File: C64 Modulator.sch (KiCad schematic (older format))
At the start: 29 parts, among them J1 Power, J2 8765, J3 4321, J4 AUD_STEREO, J5 TRS_3.5mm, J6 RCA_PLUG, Q1 BC549, Q2 BC549

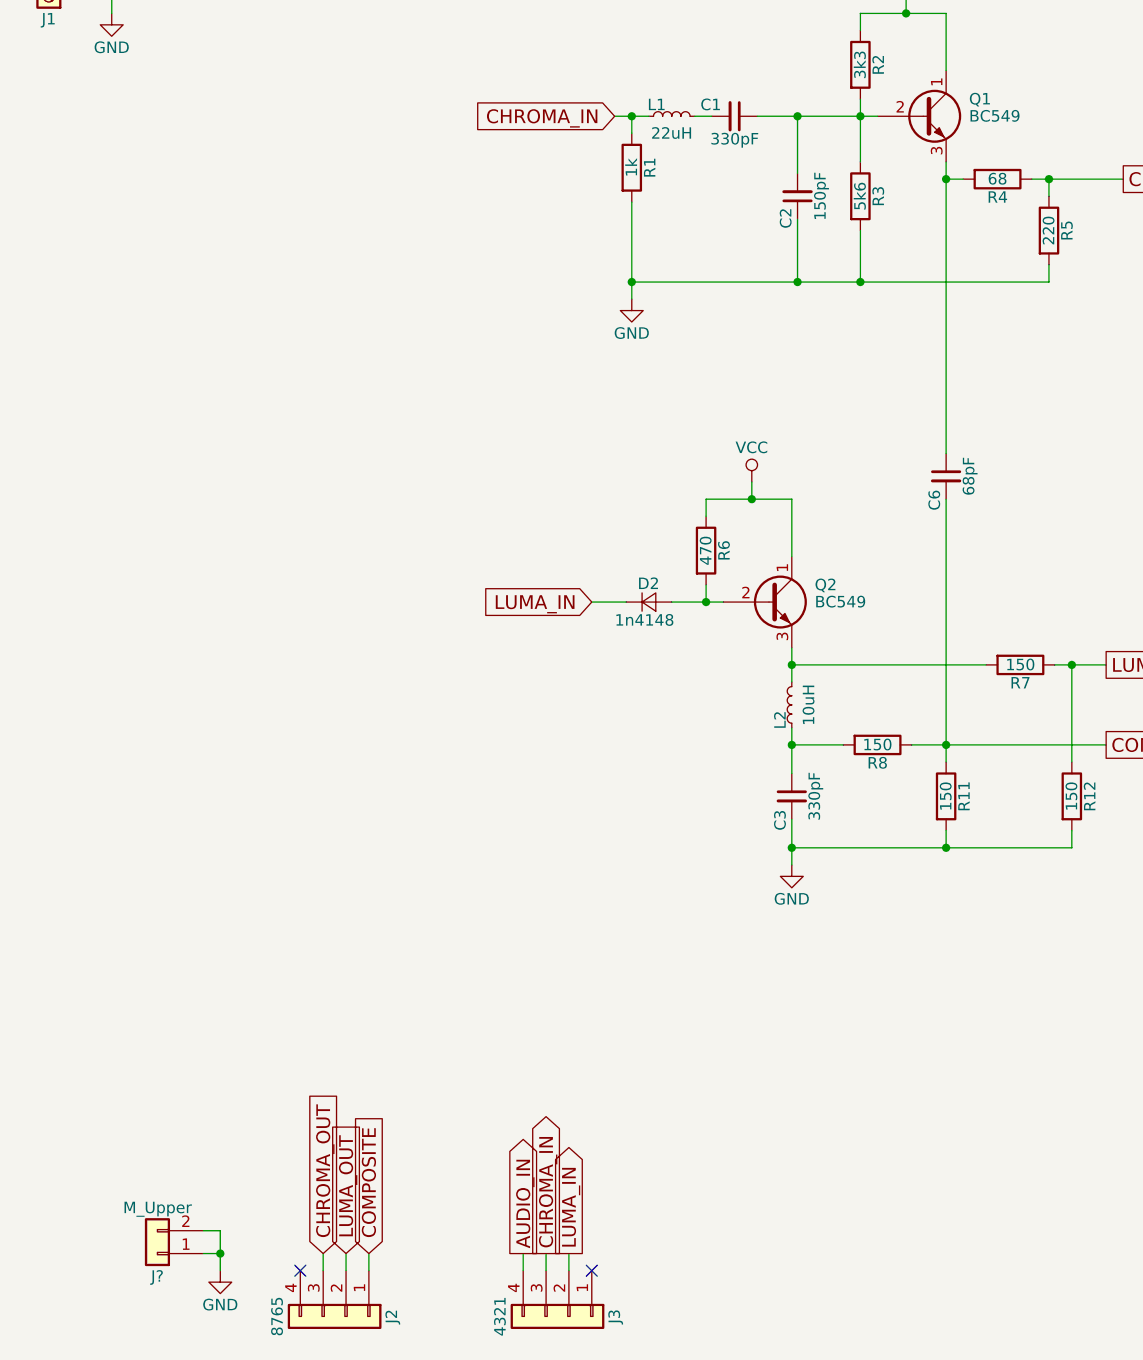
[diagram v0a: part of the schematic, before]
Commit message: Assigned footprints
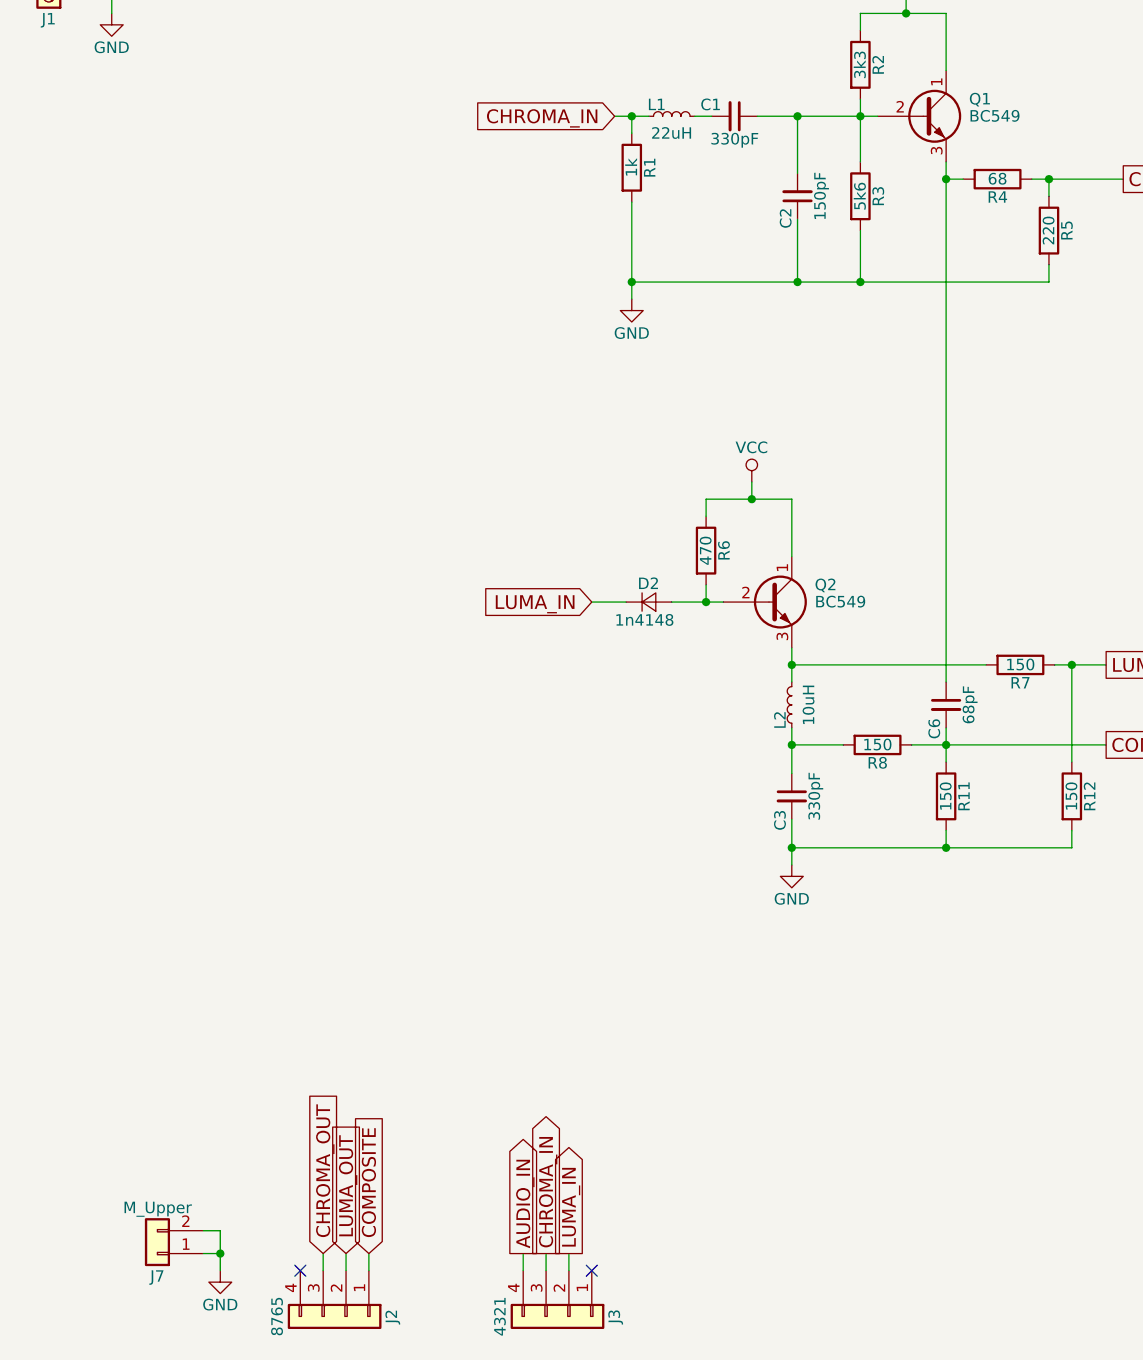
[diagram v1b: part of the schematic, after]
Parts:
- C1, C2, C3, C6: footprint (none) -> Capacitors_THT:C_Disc_D4.7mm_W2.5mm_P5.00mm
- D1, D2: footprint (none) -> Diodes_THT:D_DO-35_SOD27_P7.62mm_Horizontal
- J1, JP1: footprint (none) -> Pin_Headers:Pin_Header_Straight_1x02_Pitch2.54mm
- J2, J3: footprint (none) -> Pin_Headers:Pin_Header_Straight_1x04_Pitch2.54mm
- J4: footprint (none) -> Pin_Headers:Pin_Header_Straight_1x01_Pitch2.54mm
- J5: footprint (none) -> trs:Tayda_3.5mm_stereo_TRS_jack_A-853
- J6: footprint (none) -> rca:rca_yellow
- J7: renamed from J?; footprint (none) -> Pin_Headers:Pin_Header_Straight_1x02_Pitch2.54mm
- JP2: footprint (none) -> Pin_Headers:Pin_Header_Straight_1x03_Pitch2.54mm
- L1, L2: footprint (none) -> Inductors_THT:L_Axial_L6.6mm_D2.7mm_P10.16mm_Horizontal_Vishay_IM-2
- R1, R11, R12, R2, R3, R4, R5, R6, R7, R8: footprint (none) -> Resistors_THT:R_Axial_DIN0207_L6.3mm_D2.5mm_P10.16mm_Horizontal
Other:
- moved on the sheet: C6
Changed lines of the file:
@@
 F 0 "R2" V 5655 1350 50  0000 C CNN
 F 1 "3k3" V 5575 1350 50  0000 C CNN
-F 2 "" V 5505 1350 50  0001 C CNN
+F 2 "Resistors_THT:R_Axial_DIN0207_L6.3mm_D2.5mm_P10.16mm_Horizontal" V 5505 1350 50  0001 C CNN
 F 3 "" H 5575 1350 50  0001 C CNN
 	1    5575 1350
@@
 F 0 "R3" V 5655 1925 50  0000 C CNN
 F 1 "5k6" V 5575 1925 50  0000 C CNN
-F 2 "" V 5505 1925 50  0001 C CNN
+F 2 "Resistors_THT:R_Axial_DIN0207_L6.3mm_D2.5mm_P10.16mm_Horizontal" V 5505 1925 50  0001 C CNN
 F 3 "" H 5575 1925 50  0001 C CNN
 	1    5575 1925
@@
 F 0 "C1" V 4975 1425 50  0000 L CNN
 F 1 "330pF" V 5125 1575 50  0000 C CNN
-F 2 "" H 5025 1575 50  0001 C CNN
+F 2 "Capacitors_THT:C_Disc_D4.7mm_W2.5mm_P5.00mm" H 5025 1575 50  0001 C CNN
 F 3 "" H 5025 1575 50  0001 C CNN
 	1    5025 1575
@@
 F 0 "L1" V 4800 1600 50  0000 L CNN
 F 1 "22uH" V 4675 1575 50  0000 C CNN
-F 2 "" H 4750 1575 50  0001 C CNN
+F 2 "Inductors_THT:L_Axial_L6.6mm_D2.7mm_P10.16mm_Horizontal_Vishay_IM-2" H 4750 1575 50  0001 C CNN
 F 3 "" H 4750 1575 50  0001 C CNN
 	1    4750 1575
@@
 F 0 "R1" V 4655 1800 50  0000 C CNN
 F 1 "1k" V 4575 1800 50  0000 C CNN
-F 2 "" V 4505 1800 50  0001 C CNN
+F 2 "Resistors_THT:R_Axial_DIN0207_L6.3mm_D2.5mm_P10.16mm_Horizontal" V 4505 1800 50  0001 C CNN
 F 3 "" H 4575 1800 50  0001 C CNN
 	1    4575 1800
@@
 F 0 "C2" V 5350 1975 50  0000 L CNN
 F 1 "150pF" V 5200 1925 50  0000 C CNN
-F 2 "" H 5300 1925 50  0001 C CNN
+F 2 "Capacitors_THT:C_Disc_D4.7mm_W2.5mm_P5.00mm" H 5300 1925 50  0001 C CNN
 F 3 "" H 5300 1925 50  0001 C CNN
 	1    5300 1925
@@
 F 0 "R4" V 6255 1850 50  0000 C CNN
 F 1 "68" V 6175 1850 50  0000 C CNN
-F 2 "" V 6105 1850 50  0001 C CNN
+F 2 "Resistors_THT:R_Axial_DIN0207_L6.3mm_D2.5mm_P10.16mm_Horizontal" V 6105 1850 50  0001 C CNN
 F 3 "" H 6175 1850 50  0001 C CNN
 	1    6175 1850
@@
 $EndComp
 Wire Wire Line
-	5950 1775 5950 3050
+	5950 1775 5950 4050
 Wire Wire Line
 	5950 1850 6025 1850
@@
 F 0 "R5" V 6480 2075 50  0000 C CNN
 F 1 "220" V 6400 2075 50  0000 C CNN
-F 2 "" V 6330 2075 50  0001 C CNN
+F 2 "Resistors_THT:R_Axial_DIN0207_L6.3mm_D2.5mm_P10.16mm_Horizontal" V 6330 2075 50  0001 C CNN
 F 3 "" H 6400 2075 50  0001 C CNN
 	1    6400 2075
@@
 F 0 "R6" V 4980 3475 50  0000 C CNN
 F 1 "470" V 4900 3475 50  0000 C CNN
-F 2 "" V 4830 3475 50  0001 C CNN
+F 2 "Resistors_THT:R_Axial_DIN0207_L6.3mm_D2.5mm_P10.16mm_Horizontal" V 4830 3475 50  0001 C CNN
 F 3 "" H 4900 3475 50  0001 C CNN
 	1    4900 3475
@@
 F 0 "D2" H 4600 3780 50  0000 L CNN
 F 1 "1n4148" H 4500 3620 50  0000 L CNN
-F 2 "" V 4650 3700 50  0001 C CNN
+F 2 "Diodes_THT:D_DO-35_SOD27_P7.62mm_Horizontal" V 4650 3700 50  0001 C CNN
 F 3 "" V 4650 3700 50  0001 C CNN
 	1    4650 3700
@@
 F 0 "L2" V 5325 4175 50  0000 L CNN
 F 1 "10uH" V 5200 4150 50  0000 C CNN
-F 2 "" H 5275 4150 50  0001 C CNN
+F 2 "Inductors_THT:L_Axial_L6.6mm_D2.7mm_P10.16mm_Horizontal_Vishay_IM-2" H 5275 4150 50  0001 C CNN
 F 3 "" H 5275 4150 50  0001 C CNN
 	1    5275 4150
@@
 F 0 "D1" H 2350 1030 50  0000 L CNN
 F 1 "1n4148" H 2250 870 50  0000 L CNN
-F 2 "" V 2400 950 50  0001 C CNN
+F 2 "Diodes_THT:D_DO-35_SOD27_P7.62mm_Horizontal" V 2400 950 50  0001 C CNN
 F 3 "" V 2400 950 50  0001 C CNN
 	1    2400 950
@@
 F 0 "C3" V 5225 4400 50  0000 L CNN
 F 1 "330pF" V 5375 4550 50  0000 C CNN
-F 2 "" H 5275 4550 50  0001 C CNN
+F 2 "Capacitors_THT:C_Disc_D4.7mm_W2.5mm_P5.00mm" H 5275 4550 50  0001 C CNN
 F 3 "" H 5275 4550 50  0001 C CNN
 	1    5275 4550
@@
 F 0 "J1" H 2025 1150 50  0000 C CNN
 F 1 "Power" H 2025 850 50  0000 C CNN
-F 2 "" H 2025 1050 50  0001 C CNN
+F 2 "Pin_Headers:Pin_Header_Straight_1x02_Pitch2.54mm" H 2025 1050 50  0001 C CNN
 F 3 "" H 2025 1050 50  0001 C CNN
 	1    2025 1050
@@
 L C_Small C6
 U 1 1 5D0D1EC2
-P 5950 3150
-F 0 "C6" V 5900 3000 50  0000 L CNN
-F 1 "68pF" V 6050 3150 50  0000 C CNN
-F 2 "" H 5950 3150 50  0001 C CNN
-F 3 "" H 5950 3150 50  0001 C CNN
-	1    5950 3150
+P 5950 4150
+F 0 "C6" V 5900 4000 50  0000 L CNN
+F 1 "68pF" V 6050 4150 50  0000 C CNN
+F 2 "Capacitors_THT:C_Disc_D4.7mm_W2.5mm_P5.00mm" H 5950 4150 50  0001 C CNN
+F 3 "" H 5950 4150 50  0001 C CNN
+	1    5950 4150
 	1    0    0    -1
 $EndComp
@@
 F 0 "R11" V 6030 4550 50  0000 C CNN
 F 1 "150" V 5950 4550 50  0000 C CNN
-F 2 "" V 5880 4550 50  0001 C CNN
+F 2 "Resistors_THT:R_Axial_DIN0207_L6.3mm_D2.5mm_P10.16mm_Horizontal" V 5880 4550 50  0001 C CNN
 F 3 "" H 5950 4550 50  0001 C CNN
 	1    5950 4550
@@
 F 0 "R12" V 6580 4550 50  0000 C CNN
 F 1 "150" V 6500 4550 50  0000 C CNN
-F 2 "" V 6430 4550 50  0001 C CNN
+F 2 "Resistors_THT:R_Axial_DIN0207_L6.3mm_D2.5mm_P10.16mm_Horizontal" V 6430 4550 50  0001 C CNN
 F 3 "" H 6500 4550 50  0001 C CNN
 	1    6500 4550
@@
 F 0 "R8" V 5730 4325 50  0000 C CNN
 F 1 "150" V 5650 4325 50  0000 C CNN
-F 2 "" V 5580 4325 50  0001 C CNN
+F 2 "Resistors_THT:R_Axial_DIN0207_L6.3mm_D2.5mm_P10.16mm_Horizontal" V 5580 4325 50  0001 C CNN
 F 3 "" H 5650 4325 50  0001 C CNN
 	1    5650 4325
@@
 $EndComp
 Wire Wire Line
-	5950 3250 5950 4400
+	5950 4250 5950 4400
 Wire Wire Line
 	5800 4325 6650 4325
@@
 F 0 "R7" V 6355 3975 50  0000 C CNN
 F 1 "150" V 6275 3975 50  0000 C CNN
-F 2 "" V 6205 3975 50  0001 C CNN
+F 2 "Resistors_THT:R_Axial_DIN0207_L6.3mm_D2.5mm_P10.16mm_Horizontal" V 6205 3975 50  0001 C CNN
 F 3 "" H 6275 3975 50  0001 C CNN
 	1    6275 3975
@@
 F 0 "J3" H 4300 7025 50  0000 C CNN
 F 1 "4321" H 4300 6525 50  0000 C CNN
-F 2 "" H 4300 6825 50  0001 C CNN
+F 2 "Pin_Headers:Pin_Header_Straight_1x04_Pitch2.54mm" H 4300 6825 50  0001 C CNN
 F 3 "" H 4300 6825 50  0001 C CNN
 	1    4300 6825
@@
 F 0 "J2" H 3325 7025 50  0000 C CNN
 F 1 "8765" H 3325 6525 50  0000 C CNN
-F 2 "" H 3325 6825 50  0001 C CNN
+F 2 "Pin_Headers:Pin_Header_Straight_1x04_Pitch2.54mm" H 3325 6825 50  0001 C CNN
 F 3 "" H 3325 6825 50  0001 C CNN
 	1    3325 6825
@@
 F 0 "J6" H 10485 1420 50  0000 C CNN
 F 1 "RCA_PLUG" V 10590 1300 50  0000 C CNN
-F 2 "" H 10475 1300 50  0001 C CNN
+F 2 "rca:rca_yellow" H 10475 1300 50  0001 C CNN
 F 3 "" H 10475 1300 50  0001 C CNN
 	1    10475 1300
@@
 F 0 "J5" H 10275 2140 50  0000 C CNN
 F 1 "TRS_3.5mm" H 10125 1650 50  0000 L CNN
-F 2 "" H 10525 1950 50  0001 C CNN
+F 2 "trs:Tayda_3.5mm_stereo_TRS_jack_A-853" H 10525 1950 50  0001 C CNN
 F 3 "" H 10525 1950 50  0001 C CNN
 	1    10275 1850
@@
 F 0 "J4" H 9700 2675 50  0000 C CNN
 F 1 "AUD_STEREO" H 9700 2475 50  0000 C CNN
-F 2 "" H 9700 2575 50  0001 C CNN
+F 2 "Pin_Headers:Pin_Header_Straight_1x01_Pitch2.54mm" H 9700 2575 50  0001 C CNN
 F 3 "" H 9700 2575 50  0001 C CNN
 	1    9700 2575
@@
 F 0 "JP1" H 9200 1930 50  0000 C CNN
 F 1 "AUD_SEL" H 9210 1790 50  0000 C CNN
-F 2 "" H 9200 1850 50  0001 C CNN
+F 2 "Pin_Headers:Pin_Header_Straight_1x02_Pitch2.54mm" H 9200 1850 50  0001 C CNN
 F 3 "" H 9200 1850 50  0001 C CNN
 	1    9200 1850
@@
 F 0 "JP2" H 9750 2100 50  0000 L CNN
 F 1 "AUD_JOIN" H 9700 2300 50  0000 C BNN
-F 2 "" H 9700 2200 50  0001 C CNN
+F 2 "Pin_Headers:Pin_Header_Straight_1x03_Pitch2.54mm" H 9700 2200 50  0001 C CNN
 F 3 "" H 9700 2200 50  0001 C CNN
 	1    9700 2200
@@
 	10025 2575 9900 2575
 $Comp
-L Conn_01x02 J?
+L Conn_01x02 J7
 U 1 1 5D0E39F8
 P 2500 6550
-F 0 "J?" H 2500 6650 50  0000 C CNN
+F 0 "J7" H 2500 6650 50  0000 C CNN
 F 1 "M_Upper" H 2500 6350 50  0000 C CNN
-F 2 "" H 2500 6550 50  0001 C CNN
+F 2 "Pin_Headers:Pin_Header_Straight_1x02_Pitch2.54mm" H 2500 6550 50  0001 C CNN
 F 3 "" H 2500 6550 50  0001 C CNN
 	1    2500 6550
@@
 $EndComp
 $Comp
-L GND #PWR?
+L GND #PWR08
 U 1 1 5D0E3D58
 P 2775 6625
-F 0 "#PWR?" H 2775 6375 50  0001 C CNN
+F 0 "#PWR08" H 2775 6375 50  0001 C CNN
 F 1 "GND" H 2775 6475 50  0000 C CNN
 F 2 "" H 2775 6625 50  0001 C CNN
